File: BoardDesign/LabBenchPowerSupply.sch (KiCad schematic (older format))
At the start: 52 parts, among them P1 Digital, P2 Analog, P3 CONN_01X01, P4 CONN_01X01, P5 CONN_01X01, P6 CONN_01X01

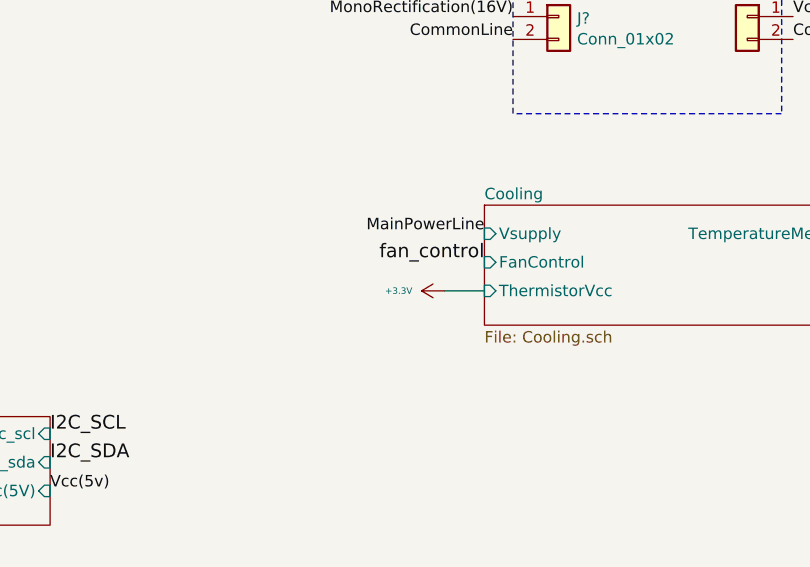
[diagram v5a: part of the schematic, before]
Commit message: Adapted thermistor divider bridge to 10k thermistor I had lying around
Signed-off-by: bebenlebricolo <benoittarrade@hotmail.fr>
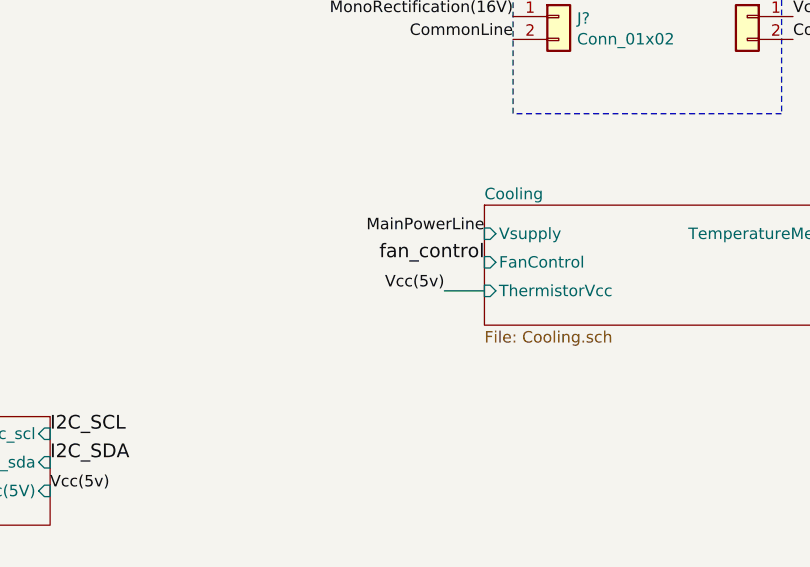
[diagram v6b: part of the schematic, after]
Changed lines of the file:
@@
 Text Notes 9100 3050 0    50   ~ 0
 Voltages measurement
-$Comp
-L power:+3V3 #PWR?
-U 1 1 5EFD4716
-P 7725 6050
-F 0 "#PWR?" H 7725 5900 50  0001 C CNN
-F 1 "+3.3V" V 7725 6250 28  0000 C CNN
-F 2 "" H 7725 6050 50  0000 C CNN
-F 3 "" H 7725 6050 50  0000 C CNN
-	1    7725 6050
-	0    -1   -1   0
-$EndComp
 Wire Wire Line
 	7725 6050 7900 6050
@@
 Text Notes 700  5875 0    31   ~ 0
 Anti collision protection circuit:\nwhen both high and low lines are triggered, \nthis transistor pulls back to ground the base of high side \nnpn driver, resulting in the extinction of high side driver, \nleaving low side driver on alone (forces N mosfets to close.\nMust reverse logic if P Mosfet is used instead of a N one)
+Text Label 7725 6050 2    50   ~ 0
+Vcc(5v)
 $EndSCHEMATC

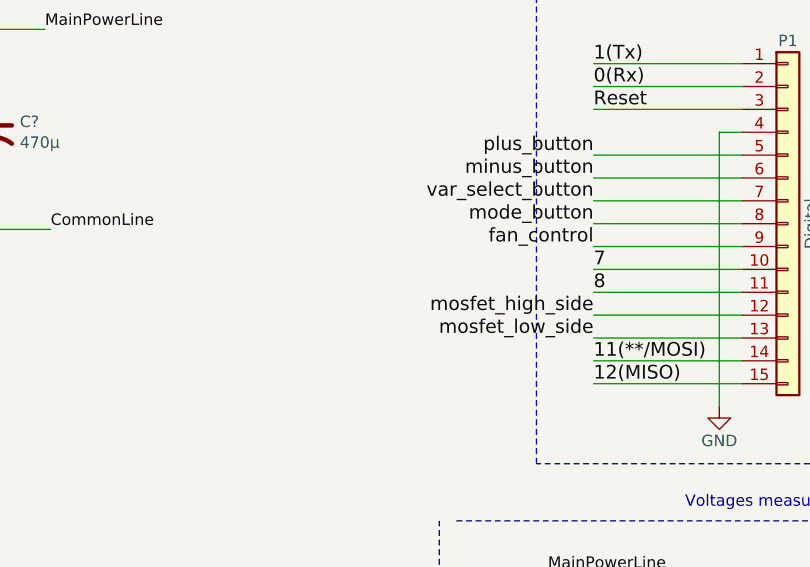
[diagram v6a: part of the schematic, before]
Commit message: Added information to PWM pins on schematic
Signed-off-by: bebenlebricolo <benoittarrade@hotmail.fr>
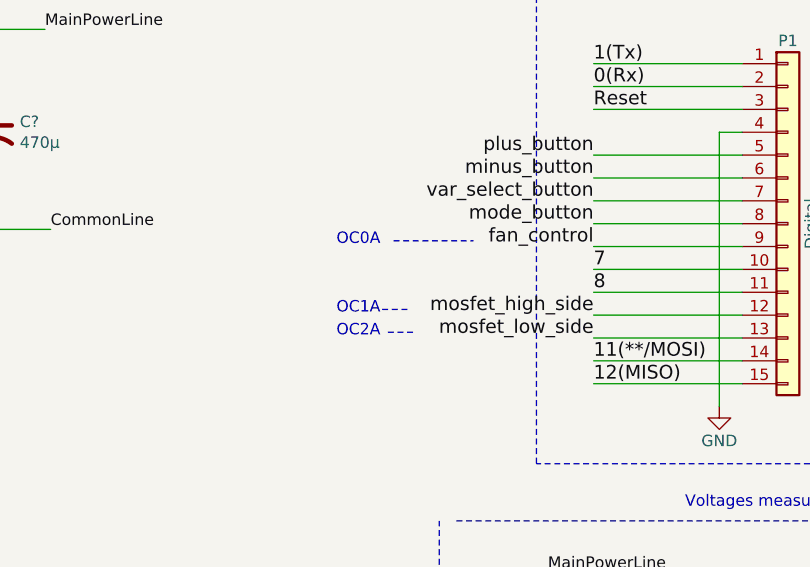
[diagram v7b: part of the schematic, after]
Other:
- note added: "OC0A"
- note added: "OC1A"
- note added: "OC2A"
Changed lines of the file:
@@
 Text Label 7725 6050 2    50   ~ 0
 Vcc(5v)
+Text Notes 7575 2200 0    50   ~ 0
+OC1A
+Text Notes 7575 2300 0    50   ~ 0
+OC2A
+Text Notes 7575 1900 0    50   ~ 0
+OC0A
+Wire Notes Line
+	7825 1875 8175 1875
+Wire Notes Line
+	7775 2175 7900 2175
+Wire Notes Line
+	7800 2275 7925 2275
 $EndSCHEMATC

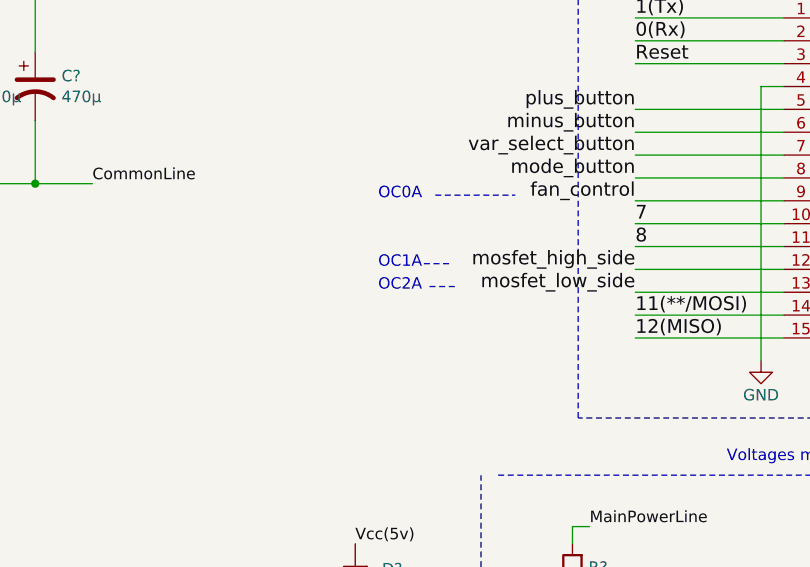
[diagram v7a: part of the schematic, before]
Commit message: Revised a bit types declaration for timers
Signed-off-by: bebenlebricolo <benoittarrade@hotmail.fr>
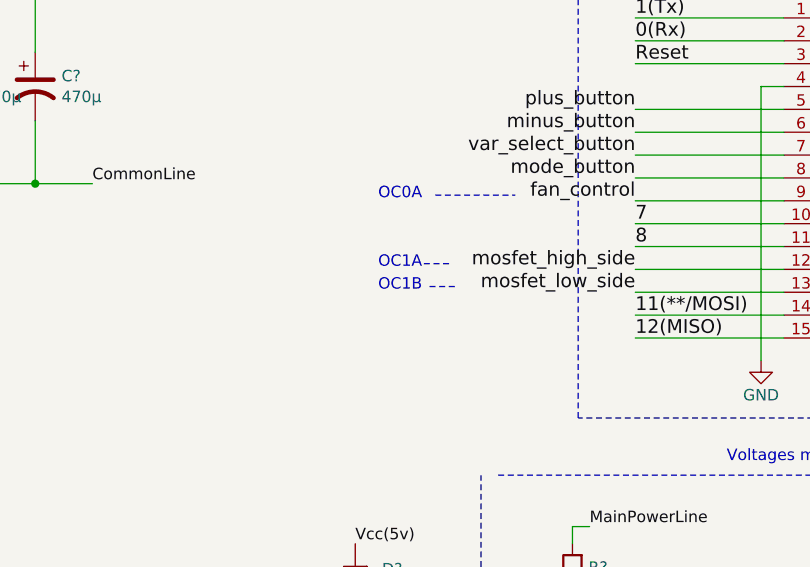
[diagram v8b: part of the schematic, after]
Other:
- note added: "OC1B"
- note removed: "OC2A"
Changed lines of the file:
@@
 OC1A
 Text Notes 7575 2300 0    50   ~ 0
-OC2A
+OC1B
 Text Notes 7575 1900 0    50   ~ 0
 OC0A
